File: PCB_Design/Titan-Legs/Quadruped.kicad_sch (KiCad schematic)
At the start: 46 parts, among them IC1 TPS54260DGQR, IC2 CP2102, J1 TYPE-C-31-M-12, P1 282837-2, SW1 SW_Push, SW2 SW_Push, T1 BC847, T2 BC847, U1 ESP32-S3-WROOM-1, U4 AMS1117-3.3

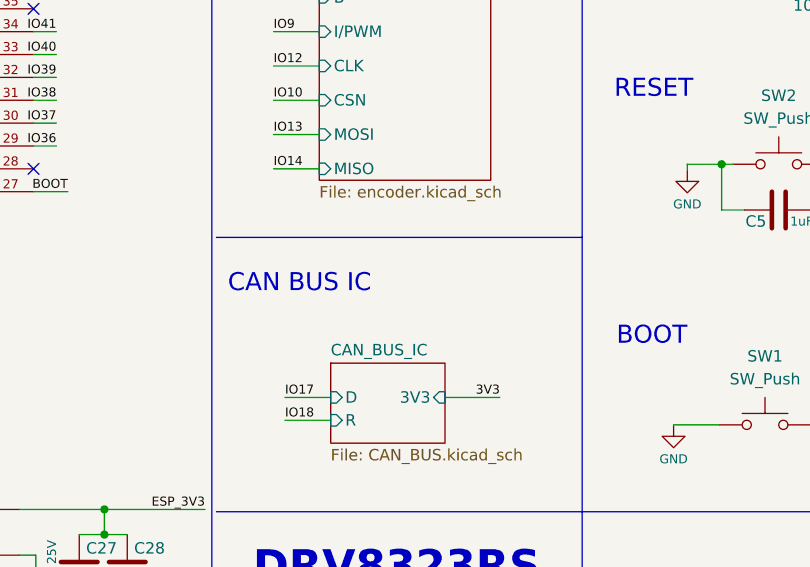
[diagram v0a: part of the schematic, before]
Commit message: Copper filled VM to mosfets
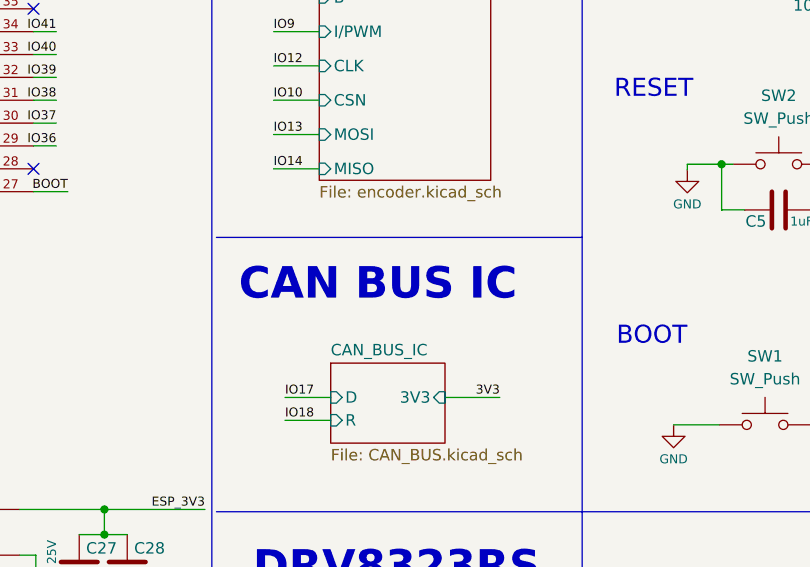
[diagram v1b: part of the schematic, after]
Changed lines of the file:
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@@
     (effects (font (size 3.5 3.5) bold) (justify left bottom))
   )
-  (text "CAN BUS IC" (at 111.76 93.98 0)
-    (effects (font (size 2 2)) (justify left bottom))
+  (text "CAN BUS IC" (at 112.9792 94.996 0)
+    (effects (font (size 3.5 3.5) (thickness 0.7) bold) (justify left bottom))
   )
   (text "TITAN LEGS" (at 126.746 25.4 0)
@@
       (reference "R10") (unit 1) (value "4.7K") (footprint "Resistor_SMD:R_0603_1608Metric")
     )
+    (path "/ee34e5ea-1d84-4f7f-ac75-7ea4a480f5c1/d1a6be26-f263-4b0c-8aa1-f0987ad122ce"
+      (reference "R11") (unit 1) (value "10K") (footprint "Resistor_SMD:R_0603_1608Metric")
+    )
     (path "/68a33b1b-c5a4-46e0-8867-0ecbab278f47"

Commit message: Add new placement for Quadruped PCB
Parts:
- D2, D3, D4: footprint LESD_diode:LESD5D50CT1G -> diodes_USB-UART:LESD5D50CT1G
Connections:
- net IO20: now reaches U1.14 (IO20)
- net IO15: now reaches U1.8 (IO15)
- net IO16: now reaches U1.9 (IO16)
- no-connect marks 28 -> 25
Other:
- sheet Miscellaneous ports: added IO20; removed none
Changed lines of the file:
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@@
   (no_connect (at 262.89 78.74))
   (no_connect (at 52.07 95.25))
-  (no_connect (at 36.83 69.85))
-  (no_connect (at 36.83 82.55))
   (no_connect (at 77.47 95.25))
   (no_connect (at 252.73 50.8))
@@
   (no_connect (at 261.62 140.97))
   (no_connect (at 262.89 73.66))
-  (no_connect (at 36.83 67.31))
   (wire (pts (xy 247.65 50.8) (xy 247.65 45.72))
     (stroke (width 0) (type default) (color 0 0 0 0))
@@
     (stroke (width 0) (type default) (color 0 0 0 0))
   )
+  (wire (pts (xy 34.29 82.55) (xy 36.83 82.55))
+    (stroke (width 0) (type default) (color 0 0 0 0))
+  )
   (wire (pts (xy 93.98 158.75) (xy 99.06 158.75))
     (stroke (width 0) (type default) (color 0 0 0 0))
@@
     (stroke (width 0) (type default) (color 0 0 0 0))
   )
+  (wire (pts (xy 34.29 69.85) (xy 36.83 69.85))
+    (stroke (width 0) (type default) (color 0 0 0 0))
+  )
   (wire (pts (xy 226.06 83.82) (xy 226.06 81.28))
     (stroke (width 0) (type default) (color 0 0 0 0))
@@
     (stroke (width 0) (type default) (color 0 0 0 0))
   )
+  (wire (pts (xy 33.02 125.73) (xy 38.1 125.73))
+    (stroke (width 0) (type default) (color 0 0 0 0))
+  )
   (wire (pts (xy 170.18 152.654) (xy 180.975 152.654))
     (stroke (width 0) (type default) (color 0 0 0 0))
@@
   )
   (polyline (pts (xy 109.22 166.37) (xy 109.22 175.26))
+    (stroke (width 0) (type default) (color 0 0 0 0))
+  )
+  (wire (pts (xy 34.29 67.31) (xy 36.83 67.31))
     (stroke (width 0) (type default) (color 0 0 0 0))
   )
@@
     (effects (font (size 1 1)) (justify left bottom))
   )
+  (label "IO20" (at 34.29 82.55 0)
+    (effects (font (size 1 1)) (justify left bottom))
+  )
   (label "IO1" (at 92.71 52.07 180)
     (effects (font (size 1 1)) (justify right bottom))
@@
     (effects (font (size 1 1)) (justify left bottom))
   )
+  (label "IO16" (at 34.29 69.85 0)
+    (effects (font (size 1 1)) (justify left bottom))
+  )
   (label "IO1" (at 144.018 153.416 180)
     (effects (font (size 1 1)) (justify right bottom))
@@
     (effects (font (size 1 1)) (justify left bottom))
   )
+  (label "IO20" (at 38.1 125.73 180)
+    (effects (font (size 1 1)) (justify right bottom))
+  )
   (label "IO40" (at 92.71 67.31 180)
     (effects (font (size 1 1)) (justify right bottom))
@@
     (effects (font (size 1 1)) (justify left bottom))
   )
-  (label "IO17" (at 144.272 139.7 180)
+  (label "IO15" (at 144.272 139.7 180)
     (effects (font (size 1 1)) (justify right bottom))
   )
@@
     (effects (font (size 1 1)) (justify left bottom))
   )
+  (label "IO15" (at 34.29 67.31 0)
+    (effects (font (size 1 1)) (justify left bottom))
+  )
   (label "3V3" (at 106.934 158.75 180)
     (effects (font (size 1 1)) (justify right bottom))
@@
     (effects (font (size 1 1)) (justify left bottom))
   )
-  (label "IO18" (at 115.57 153.924 0)
+  (label "IO16" (at 115.57 153.924 0)
     (effects (font (size 1 1)) (justify left bottom))
   )
@@
       (effects (font (size 1.27 1.27)) (justify right) hide)
     )
-    (property "Footprint" "LESD_diode:LESD5D50CT1G" (id 2) (at 187.96 137.16 0)
+    (property "Footprint" "diodes_USB-UART:LESD5D50CT1G" (id 2) (at 187.96 137.16 0)
       (effects (font (size 1.27 1.27)) (justify left bottom) hide)
     )
@@
       (effects (font (size 1.27 1.27)) (justify right) hide)
     )
-    (property "Footprint" "LESD_diode:LESD5D50CT1G" (id 2) (at 166.37 136.779 0)
+    (property "Footprint" "diodes_USB-UART:LESD5D50CT1G" (id 2) (at 166.37 136.779 0)
       (effects (font (size 1.27 1.27)) (justify left bottom) hide)
     )
@@
       (effects (font (size 1.27 1.27)) (justify right) hide)
     )
-    (property "Footprint" "LESD_diode:LESD5D50CT1G" (id 2) (at 177.165 137.16 0)
+    (property "Footprint" "diodes_USB-UART:LESD5D50CT1G" (id 2) (at 177.165 137.16 0)
       (effects (font (size 1.27 1.27)) (justify left bottom) hide)
     )
@@
       (effects (font (size 1.27 1.27)) (justify left top))
     )
+    (pin "IO20" input (at 33.02 125.73 0)
+      (effects (font (size 1.27 1.27)) (justify right))
+    )
   )
   (sheet (at 123.19 101.6) (size 12.7 8.89) (fields_autoplaced)
@@
     )
     (path "/4baa8b09-ecfb-4dcc-8570-d6fc2395af66"
-      (reference "D2") (unit 1) (value "LESD5D5.0CT1G") (footprint "LESD_diode:LESD5D50CT1G")
+      (reference "D2") (unit 1) (value "LESD5D5.0CT1G") (footprint "diodes_USB-UART:LESD5D50CT1G")
     )
     (path "/915b0835-1c62-4c66-9e90-d90b6570a880"
-      (reference "D3") (unit 1) (value "LESD5D5.0CT1G") (footprint "LESD_diode:LESD5D50CT1G")
+      (reference "D3") (unit 1) (value "LESD5D5.0CT1G") (footprint "diodes_USB-UART:LESD5D50CT1G")
     )
     (path "/4a28f097-23a1-44b5-b272-458c20ec77f5"
-      (reference "D4") (unit 1) (value "LESD5D5.0CT1G") (footprint "LESD_diode:LESD5D50CT1G")
+      (reference "D4") (unit 1) (value "LESD5D5.0CT1G") (footprint "diodes_USB-UART:LESD5D50CT1G")
     )
     (path "/983771df-a9d8-4c95-b2f8-7263116735ed/22f56f1c-46e4-43b7-94b3-1a825960510d"
@@
     )
     (path "/983771df-a9d8-4c95-b2f8-7263116735ed/2bc9c9b2-6a04-40bc-aac7-21291e4b35a9"
-      (reference "IC3") (unit 1) (value "DRV8323RSRGZT") (footprint "KiCad:QFN50P700X700X100-49N-D")
+      (reference "IC3") (unit 1) (value "DRV8323RSRGZT") (footprint "DRV8323RS:QFN50P700X700X100-49N-D")
     )
     (path "/6d0282b2-1a2b-401e-8e57-19dabb37d3cf"

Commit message: Added high voltage copper fills
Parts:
- R12, R21, R22, R3, R4, R5, R6, R7, R8, R9: footprint Resistor_SMD:R_0603_1608Metric -> Resistor_SMD:R_0402_1005Metric
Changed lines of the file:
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@@
       (effects (font (size 1 1)) (justify left))
     )
-    (property "Footprint" "Resistor_SMD:R_0603_1608Metric" (id 2) (at 243.332 107.95 90)
+    (property "Footprint" "Resistor_SMD:R_0402_1005Metric" (id 2) (at 243.332 107.95 90)
       (effects (font (size 1.27 1.27)) hide)
     )
@@
       (effects (font (size 1 1)) (justify left))
     )
-    (property "Footprint" "Resistor_SMD:R_0603_1608Metric" (id 2) (at 179.832 103.378 90)
+    (property "Footprint" "Resistor_SMD:R_0402_1005Metric" (id 2) (at 179.832 103.378 90)
       (effects (font (size 1.27 1.27)) hide)
     )
@@
       (effects (font (size 0.762 0.762)))
     )
-    (property "Footprint" "Resistor_SMD:R_0603_1608Metric" (id 2) (at 267.97 152.273 90)
+    (property "Footprint" "Resistor_SMD:R_0402_1005Metric" (id 2) (at 267.97 152.273 90)
       (effects (font (size 1.27 1.27)) hide)
     )
@@
       (effects (font (size 1 1)) (justify left))
     )
-    (property "Footprint" "Resistor_SMD:R_0603_1608Metric" (id 2) (at 238.252 107.95 90)
+    (property "Footprint" "Resistor_SMD:R_0402_1005Metric" (id 2) (at 238.252 107.95 90)
       (effects (font (size 1.27 1.27)) hide)
     )
@@
       (effects (font (size 1 1)))
     )
-    (property "Footprint" "Resistor_SMD:R_0603_1608Metric" (id 2) (at 221.742 137.16 90)
+    (property "Footprint" "Resistor_SMD:R_0402_1005Metric" (id 2) (at 221.742 137.16 90)
       (effects (font (size 1.27 1.27)) hide)
     )
@@
       (effects (font (size 1 1)) (justify left))
     )
-    (property "Footprint" "Resistor_SMD:R_0603_1608Metric" (id 2) (at 222.758 111.76 90)
+    (property "Footprint" "Resistor_SMD:R_0402_1005Metric" (id 2) (at 222.758 111.76 90)
       (effects (font (size 1.27 1.27)) hide)
     )
@@
       (effects (font (size 1.27 1.27)) (justify left))
     )
-    (property "Footprint" "Resistor_SMD:R_0603_1608Metric" (id 2) (at 176.022 42.164 90)
+    (property "Footprint" "Resistor_SMD:R_0402_1005Metric" (id 2) (at 176.022 42.164 90)
       (effects (font (size 1.27 1.27)) hide)
     )
@@
       (effects (font (size 1.27 1.27)) (justify left))
     )
-    (property "Footprint" "Resistor_SMD:R_0603_1608Metric" (id 2) (at 176.022 60.96 90)
+    (property "Footprint" "Resistor_SMD:R_0402_1005Metric" (id 2) (at 176.022 60.96 90)
       (effects (font (size 1.27 1.27)) hide)
     )
@@
       (effects (font (size 1 1)) (justify left))
     )
-    (property "Footprint" "Resistor_SMD:R_0603_1608Metric" (id 2) (at 218.694 107.188 90)
+    (property "Footprint" "Resistor_SMD:R_0402_1005Metric" (id 2) (at 218.694 107.188 90)
       (effects (font (size 1.27 1.27)) hide)
     )
@@
       (effects (font (size 1 1)) (justify left))
     )
-    (property "Footprint" "Resistor_SMD:R_0603_1608Metric" (id 2) (at 181.356 74.422 90)
+    (property "Footprint" "Resistor_SMD:R_0402_1005Metric" (id 2) (at 181.356 74.422 90)
       (effects (font (size 1.27 1.27)) hide)
     )
@@
     )
     (path "/983771df-a9d8-4c95-b2f8-7263116735ed/22f56f1c-46e4-43b7-94b3-1a825960510d"
-      (reference "D5") (unit 1) (value "LED") (footprint "LED_SMD:LED_0603_1608Metric")
+      (reference "D5") (unit 1) (value "LED") (footprint "LED_SMD:LED_0402_1005Metric")
     )
     (path "/fddf2939-6581-4168-83e6-bfc5e62b7a8a"
@@
     )
     (path "/c3656d41-d7bf-48cb-9af8-809c8e4738b0"
-      (reference "R3") (unit 1) (value "10k") (footprint "Resistor_SMD:R_0603_1608Metric")
+      (reference "R3") (unit 1) (value "10k") (footprint "Resistor_SMD:R_0402_1005Metric")
     )
     (path "/ce7e89e4-d131-4df5-ae3a-b8ce628ec329"
-      (reference "R4") (unit 1) (value "10k") (footprint "Resistor_SMD:R_0603_1608Metric")
+      (reference "R4") (unit 1) (value "10k") (footprint "Resistor_SMD:R_0402_1005Metric")
     )
     (path "/3ccd31a4-1b3d-4977-97dc-c77607d03375"
-      (reference "R5") (unit 1) (value "10K") (footprint "Resistor_SMD:R_0603_1608Metric")
+      (reference "R5") (unit 1) (value "10K") (footprint "Resistor_SMD:R_0402_1005Metric")
     )
     (path "/ed613605-d50e-41a7-b8f2-f60c392b4bc5"
-      (reference "R6") (unit 1) (value "10K") (footprint "Resistor_SMD:R_0603_1608Metric")
+      (reference "R6") (unit 1) (value "10K") (footprint "Resistor_SMD:R_0402_1005Metric")
     )
     (path "/927635cd-1948-4290-9280-1d70ef3bbba3"
-      (reference "R7") (unit 1) (value "5.1k") (footprint "Resistor_SMD:R_0603_1608Metric")
+      (reference "R7") (unit 1) (value "5.1k") (footprint "Resistor_SMD:R_0402_1005Metric")
     )
     (path "/7f314f4f-bdf4-4bb6-a4f5-e4fcfac7d1ad"
-      (reference "R8") (unit 1) (value "1K") (footprint "Resistor_SMD:R_0603_1608Metric")
+      (reference "R8") (unit 1) (value "1K") (footprint "Resistor_SMD:R_0402_1005Metric")
     )
     (path "/3bbdef38-e092-4205-8641-a95f347e4dc0"
-      (reference "R9") (unit 1) (value "10K") (footprint "Resistor_SMD:R_0603_1608Metric")
+      (reference "R9") (unit 1) (value "10K") (footprint "Resistor_SMD:R_0402_1005Metric")
     )
     (path "/b23984b5-9f54-4356-8a16-c3212b50a2a0/ca410c7b-44b9-4164-b021-bbf1896d7bc4"
@@
     )
     (path "/68a33b1b-c5a4-46e0-8867-0ecbab278f47"
-      (reference "R12") (unit 1) (value "5.1k") (footprint "Resistor_SMD:R_0603_1608Metric")
+      (reference "R12") (unit 1) (value "5.1k") (footprint "Resistor_SMD:R_0402_1005Metric")
     )
     (path "/eb34d206-56ca-44ca-9e9b-c8513ecb240f/6fef41bf-697e-4d5b-9684-0d857b9965a7"
-      (reference "R13") (unit 1) (value "10K") (footprint "Resistor_SMD:R_0603_1608Metric")
+      (reference "R13") (unit 1) (value "10K") (footprint "Resistor_SMD:R_0402_1005Metric")
     )
     (path "/983771df-a9d8-4c95-b2f8-7263116735ed/1616499b-6a69-425e-b8fa-e342d6d49a89"
@@
     )
     (path "/983771df-a9d8-4c95-b2f8-7263116735ed/8a826e4e-2fbc-4ff3-8fa2-79566921b526"
-      (reference "R17") (unit 1) (value "330") (footprint "Resistor_SMD:R_0603_1608Metric")
+      (reference "R17") (unit 1) (value "330") (footprint "Resistor_SMD:R_0402_1005Metric")
     )
     (path "/983771df-a9d8-4c95-b2f8-7263116735ed/3b61b910-0804-4756-b382-a4e95f07c3e7"
-      (reference "R18") (unit 1) (value "10k") (footprint "Resistor_SMD:R_0603_1608Metric")
+      (reference "R18") (unit 1) (value "10k") (footprint "Resistor_SMD:R_0402_1005Metric")
     )
     (path "/eb4a6687-cba5-448e-acce-d7bcbebf069b"
-      (reference "R21") (unit 1) (value "22.1K") (footprint "Resistor_SMD:R_0603_1608Metric")
+      (reference "R21") (unit 1) (value "22.1K") (footprint "Resistor_SMD:R_0402_1005Metric")
     )
     (path "/990841ca-d305-4b42-8529-e17ddf1df628"
-      (reference "R22") (unit 1) (value "47.5K") (footprint "Resistor_SMD:R_0603_1608Metric")
+      (reference "R22") (unit 1) (value "47.5K") (footprint "Resistor_SMD:R_0402_1005Metric")
     )
     (path "/685b7ea4-0e36-4b4e-98e9-e356cbba78be"

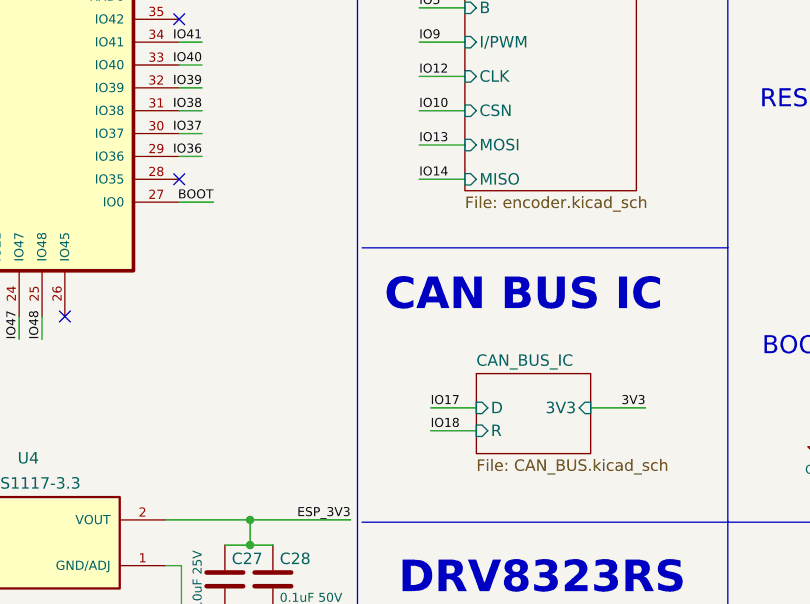
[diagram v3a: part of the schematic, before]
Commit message: Added DRV8323RS Traces and some minor changes
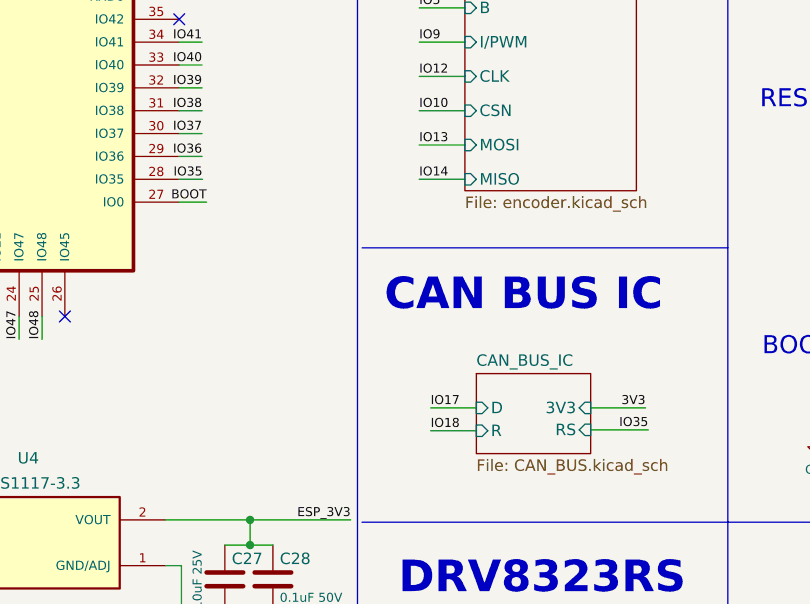
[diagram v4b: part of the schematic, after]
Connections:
- net IO35: now reaches U1.28 (IO35)
- no-connect marks 25 -> 24
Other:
- sheet CAN_BUS_IC ports: added RS; removed none
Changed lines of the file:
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@@
   (no_connect (at 252.73 104.14))
   (no_connect (at 242.57 50.8))
-  (no_connect (at 90.17 80.01))
   (no_connect (at 247.65 104.14))
   (no_connect (at 229.87 68.58))
@@
     (stroke (width 0) (type default) (color 0 0 0 0))
   )
+  (wire (pts (xy 90.17 80.01) (xy 92.7608 80.01))
+    (stroke (width 0) (type default) (color 0 0 0 0))
+  )
   (wire (pts (xy 98.044 128.27) (xy 98.044 129.54))
     (stroke (width 0) (type default) (color 0 0 0 0))
@@
     (stroke (width 0) (type default) (color 0 0 0 0))
   )
-  (wire (pts (xy 90.17 82.55) (xy 93.98 82.55))
+  (wire (pts (xy 90.17 82.55) (xy 93.218 82.55))
     (stroke (width 0) (type default) (color 0 0 0 0))
   )
@@
   )
   (wire (pts (xy 140.8684 181.4068) (xy 140.8684 183.7436))
+    (stroke (width 0) (type default) (color 0 0 0 0))
+  )
+  (wire (pts (xy 135.89 107.8484) (xy 142.2908 107.8484))
     (stroke (width 0) (type default) (color 0 0 0 0))
   )
@@
     (effects (font (size 1 1)) (justify right bottom))
   )
+  (label "IO35" (at 92.7608 80.01 180)
+    (effects (font (size 1 1)) (justify right bottom))
+  )
   (label "D-" (at 214.63 146.05 0)
     (effects (font (size 1 1)) (justify left bottom))
@@
     (effects (font (size 1 1)) (justify right bottom))
   )
+  (label "IO35" (at 142.2908 107.8484 180)
+    (effects (font (size 1 1)) (justify right bottom))
+  )
   (label "IO48" (at 74.93 97.79 90)
     (effects (font (size 1 1)) (justify left bottom))
@@
     (effects (font (size 1 1)) (justify right bottom))
   )
-  (label "BOOT" (at 93.98 82.55 180)
+  (label "BOOT" (at 93.218 82.55 180)
     (effects (font (size 1 1)) (justify right bottom))
   )
@@
       (effects (font (size 1.27 1.27)) (justify right))
     )
+    (pin "RS" input (at 135.89 107.8484 0)
+      (effects (font (size 1.27 1.27)) (justify right))
+    )
